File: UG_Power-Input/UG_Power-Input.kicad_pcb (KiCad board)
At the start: 2 copper layers, 109.2 x 68.6 mm, 46 parts, among them J1 12V IN, J2 12V OUT, J3 5V OUT, U1 LM2679

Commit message: PCB rendering added
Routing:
- net GND: vias 120 -> 166
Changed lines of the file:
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@@
     (thickness 1.6002)
     (drawings 66)
-    (tracks 132)
+    (tracks 178)
     (zones 0)
     (modules 46)
@@
     (38 B.Mask user)
     (39 F.Mask user)
+    (41 Cmts.User user)
     (44 Edge.Cuts user)
     (45 Margin user)
-    (46 B.CrtYd user)
-    (47 F.CrtYd user)
+    (46 B.CrtYd user hide)
+    (47 F.CrtYd user hide)
     (49 F.Fab user hide)
   )
@@
     (solder_mask_min_width 0.1)
     (aux_axis_origin 102.87 62.484)
-    (grid_origin 102.87 62.484)
+    (grid_origin 209.042 100.076)
     (visible_elements FFFFFFFF)
     (pcbplotparams
@@
     (tags "mounting hole 3.5mm")
     (attr virtual)
-    (fp_text reference H3 (at 5.334 0) (layer B.SilkS)
-      (effects (font (size 1 1) (thickness 0.15)) (justify mirror))
-    )
-    (fp_text value 3.5mm (at 6.858 0) (layer F.SilkS)
+    (fp_text reference H3 (at 5.334 0.762) (layer B.SilkS)
+      (effects (font (size 1 1) (thickness 0.15)) (justify mirror))
+    )
+    (fp_text value 3.5mm (at 6.858 0.762) (layer F.SilkS)
       (effects (font (size 1 1) (thickness 0.15)))
     )
@@
   (gr_line (start 119.126 94.234) (end 119.126 86.106) (layer B.SilkS) (width 0.3))
   (gr_line (start 111.252 94.234) (end 119.126 94.234) (layer B.SilkS) (width 0.3))
-  (dimension 68.58 (width 0.1524) (layer F.Fab)
-    (gr_text "68.580 mm" (at 218.4908 96.774 270) (layer F.Fab)
+  (dimension 68.58 (width 0.1524) (layer Cmts.User)
+    (gr_text "68.580 mm" (at 218.4908 96.774 -90) (layer Cmts.User)
       (effects (font (size 1.016 1.016) (thickness 0.1524)))
     )
@@
     (arrow2b (pts (xy 217.17 62.484) (xy 217.756421 63.610504)))
   )
-  (dimension 109.22 (width 0.1524) (layer F.Fab)
-    (gr_text "109.220 mm" (at 157.48 56.0832) (layer F.Fab)
+  (dimension 109.22 (width 0.1524) (layer Cmts.User)
+    (gr_text "109.220 mm" (at 157.48 56.0832) (layer Cmts.User)
       (effects (font (size 1.016 1.016) (thickness 0.1524)))
     )
@@
   (via (at 209.042 102.616) (size 0.8) (drill 0.4) (layers Front Back) (net 1))
   (via (at 209.042 100.076) (size 0.8) (drill 0.4) (layers Front Back) (net 1))
-  (via (at 203.962 95.758) (size 0.8) (drill 0.4) (layers Front Back) (net 1))
-  (via (at 203.962 90.678) (size 0.8) (drill 0.4) (layers Front Back) (net 1))
-  (via (at 206.502 98.298) (size 0.8) (drill 0.4) (layers Front Back) (net 1))
-  (via (at 203.962 88.138) (size 0.8) (drill 0.4) (layers Front Back) (net 1))
+  (via (at 203.962 94.996) (size 0.8) (drill 0.4) (layers Front Back) (net 1))
+  (via (at 203.962 89.916) (size 0.8) (drill 0.4) (layers Front Back) (net 1))
+  (via (at 206.502 97.536) (size 0.8) (drill 0.4) (layers Front Back) (net 1))
+  (via (at 203.962 87.376) (size 0.8) (drill 0.4) (layers Front Back) (net 1))
   (via (at 201.422 83.058) (size 0.8) (drill 0.4) (layers Front Back) (net 1))
   (via (at 203.962 80.518) (size 0.8) (drill 0.4) (layers Front Back) (net 1))
   (via (at 206.502 77.978) (size 0.8) (drill 0.4) (layers Front Back) (net 1))
-  (via (at 206.502 72.898) (size 0.8) (drill 0.4) (layers Front Back) (net 1))
+  (via (at 206.502 72.136) (size 0.8) (drill 0.4) (layers Front Back) (net 1))
   (via (at 197.104 67.564) (size 0.8) (drill 0.4) (layers Front Back) (net 1))
   (via (at 199.644 67.564) (size 0.8) (drill 0.4) (layers Front Back) (net 1))
   (via (at 202.184 67.564) (size 0.8) (drill 0.4) (layers Front Back) (net 1))
   (via (at 197.104 65.024) (size 0.8) (drill 0.4) (layers Front Back) (net 1))
+  (via (at 135.128 64.516) (size 0.8) (drill 0.4) (layers Front Back) (net 1))
+  (via (at 132.588 64.516) (size 0.8) (drill 0.4) (layers Front Back) (net 1))
+  (via (at 130.048 64.516) (size 0.8) (drill 0.4) (layers Front Back) (net 1))
+  (via (at 127.508 64.516) (size 0.8) (drill 0.4) (layers Front Back) (net 1))
+  (via (at 124.968 64.516) (size 0.8) (drill 0.4) (layers Front Back) (net 1))
+  (via (at 122.428 64.516) (size 0.8) (drill 0.4) (layers Front Back) (net 1))
+  (via (at 119.888 64.516) (size 0.8) (drill 0.4) (layers Front Back) (net 1))
+  (via (at 117.348 64.516) (size 0.8) (drill 0.4) (layers Front Back) (net 1))
+  (via (at 114.808 64.516) (size 0.8) (drill 0.4) (layers Front Back) (net 1))
+  (via (at 112.268 64.516) (size 0.8) (drill 0.4) (layers Front Back) (net 1))
+  (via (at 112.268 67.056) (size 0.8) (drill 0.4) (layers Front Back) (net 1))
+  (via (at 112.268 69.596) (size 0.8) (drill 0.4) (layers Front Back) (net 1))
+  (via (at 112.268 72.136) (size 0.8) (drill 0.4) (layers Front Back) (net 1))
+  (via (at 109.728 72.136) (size 0.8) (drill 0.4) (layers Front Back) (net 1))
+  (via (at 107.188 72.136) (size 0.8) (drill 0.4) (layers Front Back) (net 1))
+  (via (at 104.648 72.136) (size 0.8) (drill 0.4) (layers Front Back) (net 1))
+  (via (at 104.648 74.676) (size 0.8) (drill 0.4) (layers Front Back) (net 1))
+  (via (at 104.648 77.216) (size 0.8) (drill 0.4) (layers Front Back) (net 1))
+  (via (at 135.128 129.032) (size 0.8) (drill 0.4) (layers Front Back) (net 1))
+  (via (at 132.588 129.032) (size 0.8) (drill 0.4) (layers Front Back) (net 1))
+  (via (at 130.048 129.032) (size 0.8) (drill 0.4) (layers Front Back) (net 1))
+  (via (at 127.508 129.032) (size 0.8) (drill 0.4) (layers Front Back) (net 1))
+  (via (at 124.968 129.032) (size 0.8) (drill 0.4) (layers Front Back) (net 1))
+  (via (at 122.428 129.032) (size 0.8) (drill 0.4) (layers Front Back) (net 1))
+  (via (at 119.888 129.032) (size 0.8) (drill 0.4) (layers Front Back) (net 1))
+  (via (at 117.348 129.032) (size 0.8) (drill 0.4) (layers Front Back) (net 1))
+  (via (at 114.808 129.032) (size 0.8) (drill 0.4) (layers Front Back) (net 1))
+  (via (at 112.268 129.032) (size 0.8) (drill 0.4) (layers Front Back) (net 1))
+  (via (at 112.268 126.492) (size 0.8) (drill 0.4) (layers Front Back) (net 1))
+  (via (at 112.268 123.952) (size 0.8) (drill 0.4) (layers Front Back) (net 1))
+  (via (at 112.268 121.412) (size 0.8) (drill 0.4) (layers Front Back) (net 1))
+  (via (at 109.728 121.412) (size 0.8) (drill 0.4) (layers Front Back) (net 1))
+  (via (at 104.648 121.412) (size 0.8) (drill 0.4) (layers Front Back) (net 1))
+  (via (at 104.648 118.872) (size 0.8) (drill 0.4) (layers Front Back) (net 1))
+  (via (at 104.648 116.332) (size 0.8) (drill 0.4) (layers Front Back) (net 1))
+  (via (at 158.75 129.032) (size 0.8) (drill 0.4) (layers Front Back) (net 1))
+  (via (at 161.29 129.032) (size 0.8) (drill 0.4) (layers Front Back) (net 1))
+  (via (at 163.83 129.032) (size 0.8) (drill 0.4) (layers Front Back) (net 1))
+  (via (at 209.042 97.536) (size 0.8) (drill 0.4) (layers Front Back) (net 1))
+  (via (at 209.042 94.996) (size 0.8) (drill 0.4) (layers Front Back) (net 1))
+  (via (at 209.042 89.916) (size 0.8) (drill 0.4) (layers Front Back) (net 1))
+  (via (at 209.042 87.376) (size 0.8) (drill 0.4) (layers Front Back) (net 1))
+  (via (at 209.042 84.836) (size 0.8) (drill 0.4) (layers Front Back) (net 1))
+  (via (at 209.042 79.756) (size 0.8) (drill 0.4) (layers Front Back) (net 1))
+  (via (at 209.042 77.216) (size 0.8) (drill 0.4) (layers Front Back) (net 1))
+  (via (at 209.042 72.136) (size 0.8) (drill 0.4) (layers Front Back) (net 1))
   (segment (start 193.294 110.744) (end 196.088 110.744) (width 2) (layer Front) (net 3))
   (segment (start 193.294 115.824) (end 196.088 115.824) (width 2) (layer Front) (net 5))
@@
     (polygon
       (pts
-        (xy 122.428 96.52) (xy 103.378 96.52) (xy 103.378 80.772) (xy 122.428 80.772)
+        (xy 122.428 96.52) (xy 102.87 96.52) (xy 102.87 80.772) (xy 122.428 80.772)
       )
     )
@@
     (polygon
       (pts
-        (xy 122.428 112.776) (xy 103.378 112.776) (xy 103.378 97.028) (xy 122.428 97.028)
+        (xy 122.428 112.776) (xy 102.87 112.776) (xy 102.87 97.028) (xy 122.428 97.028)
       )
     )

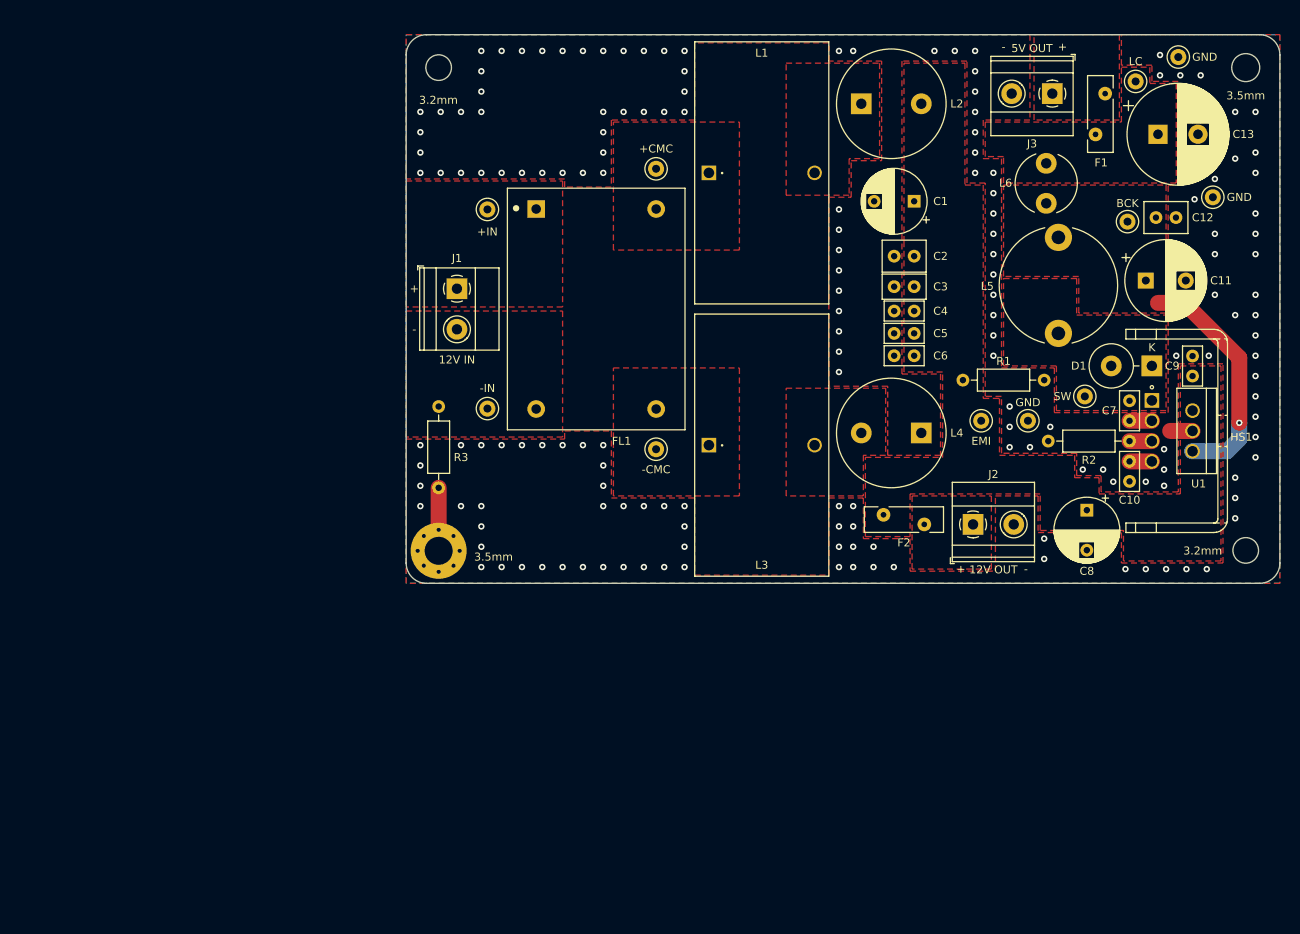
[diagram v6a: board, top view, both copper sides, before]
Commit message: Changes to terminal blocks
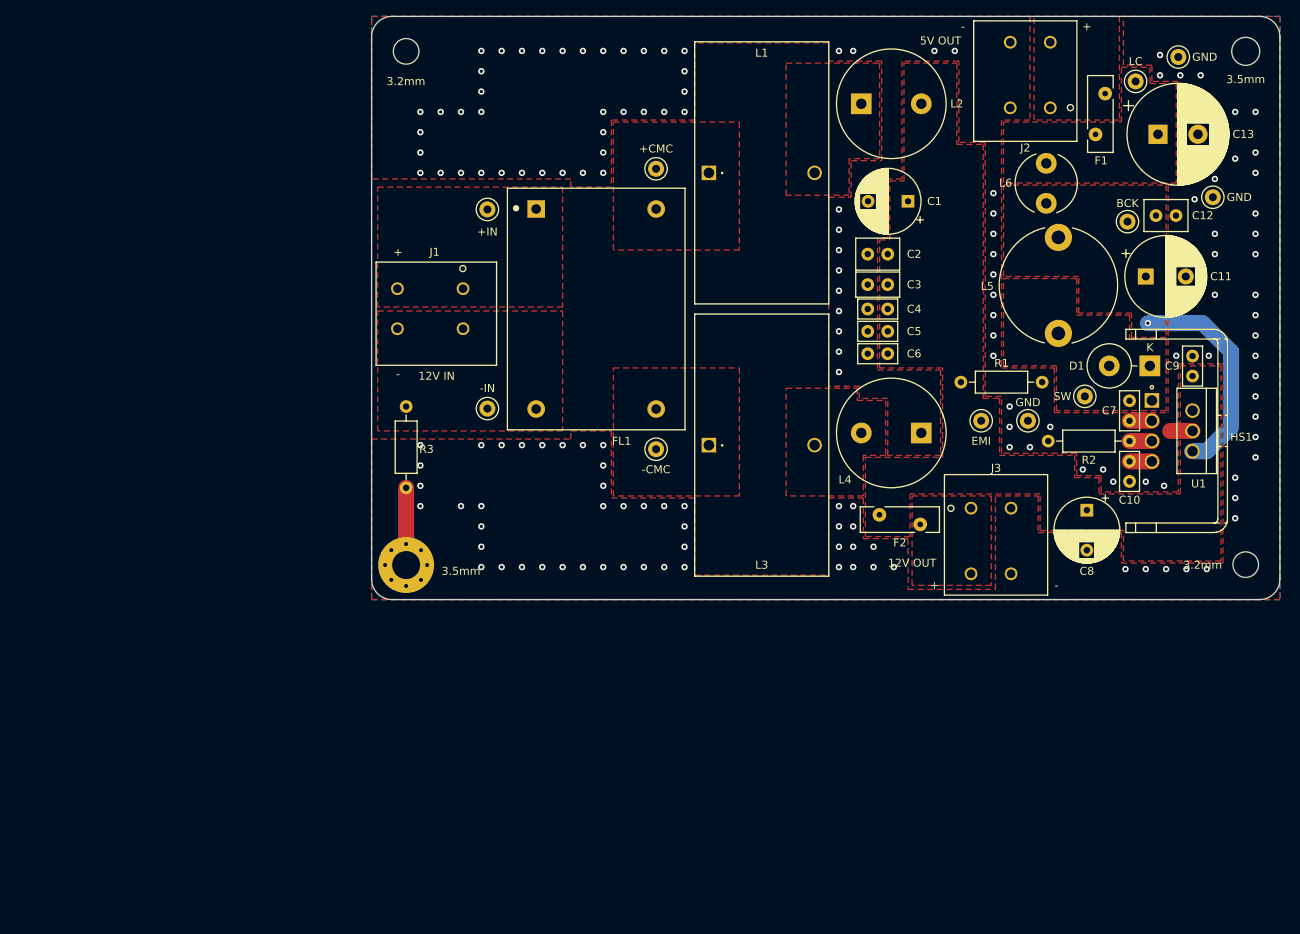
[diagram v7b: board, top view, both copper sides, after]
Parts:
- J1: footprint TerminalBlock_Phoenix:TerminalBlock_Phoenix_MKDS-1,5-2-5.08_1x02_P5.08mm_Horizontal -> TerminalBlock_Weidemueller:TerminalBlock_Weidemueller_LMF-1330180000_1x02_P5.00mm_Vertical
- J2: value 12V OUT -> 5V OUT; footprint TerminalBlock_Phoenix:TerminalBlock_Phoenix_MKDS-1,5-2-5.08_1x02_P5.08mm_Horizontal -> TerminalBlock_Weidemueller:TerminalBlock_Weidemueller_LMF-1330180000_1x02_P5.00mm_Vertical
- J3: value 5V OUT -> 12V OUT; footprint TerminalBlock_Phoenix:TerminalBlock_Phoenix_MKDS-1,5-2-5.08_1x02_P5.08mm_Horizontal -> TerminalBlock_Weidemueller:TerminalBlock_Weidemueller_LMF-1330180000_1x02_P5.00mm_Vertical
- moved J2 53.0 mm to (183.4, 71.6), turned to 180 degrees
- moved J3 52.8 mm to (173.5, 121.7), turned to 0 degrees
- moved H1 4.54 mm to (102.9, 64.6)
- moved H3 4.44 mm to (102.9, 128.8)
- moved R3 4.06 mm to (102.9, 109.0)
- moved C2 3.31 mm to (163.1, 89.9)
- moved C3 3.31 mm to (163.1, 93.7)
- moved C4 3.31 mm to (163.1, 96.8)
- moved C5 3.31 mm to (163.1, 99.6)
- moved C6 3.31 mm to (163.1, 102.4)
- moved H2 2.03 mm to (207.8, 64.6)
- moved H4 1.78 mm to (207.8, 128.7)
- moved C1 0.76 mm to (165.6, 83.3)
- moved J1 0.76 mm to (110.0, 94.2)
- moved C11 0.51 mm to (195.3, 92.7)
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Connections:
- J1 pad 2: -IN -> Net-(FL1-Pad1)
- J2 pad 1: Net-(F2-Pad1) -> Net-(F1-Pad1)
- J2 pad 2: GND -> Net-(F1-Pad1)
- J3 pad 1: Net-(F1-Pad1) -> Net-(F2-Pad1)
- J3 pad 2: GND -> Net-(F2-Pad1)
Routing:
- net BUCK.OUT: track 29.7 -> 27.4 mm
- net Net-(H3-Pad1): track 7.82 -> 9.65 mm
- net GND: vias 166 -> 152
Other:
- board size 109.2 x 68.6 mm -> 113.5 x 72.9 mm

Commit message: Changes to PCB silkscreen
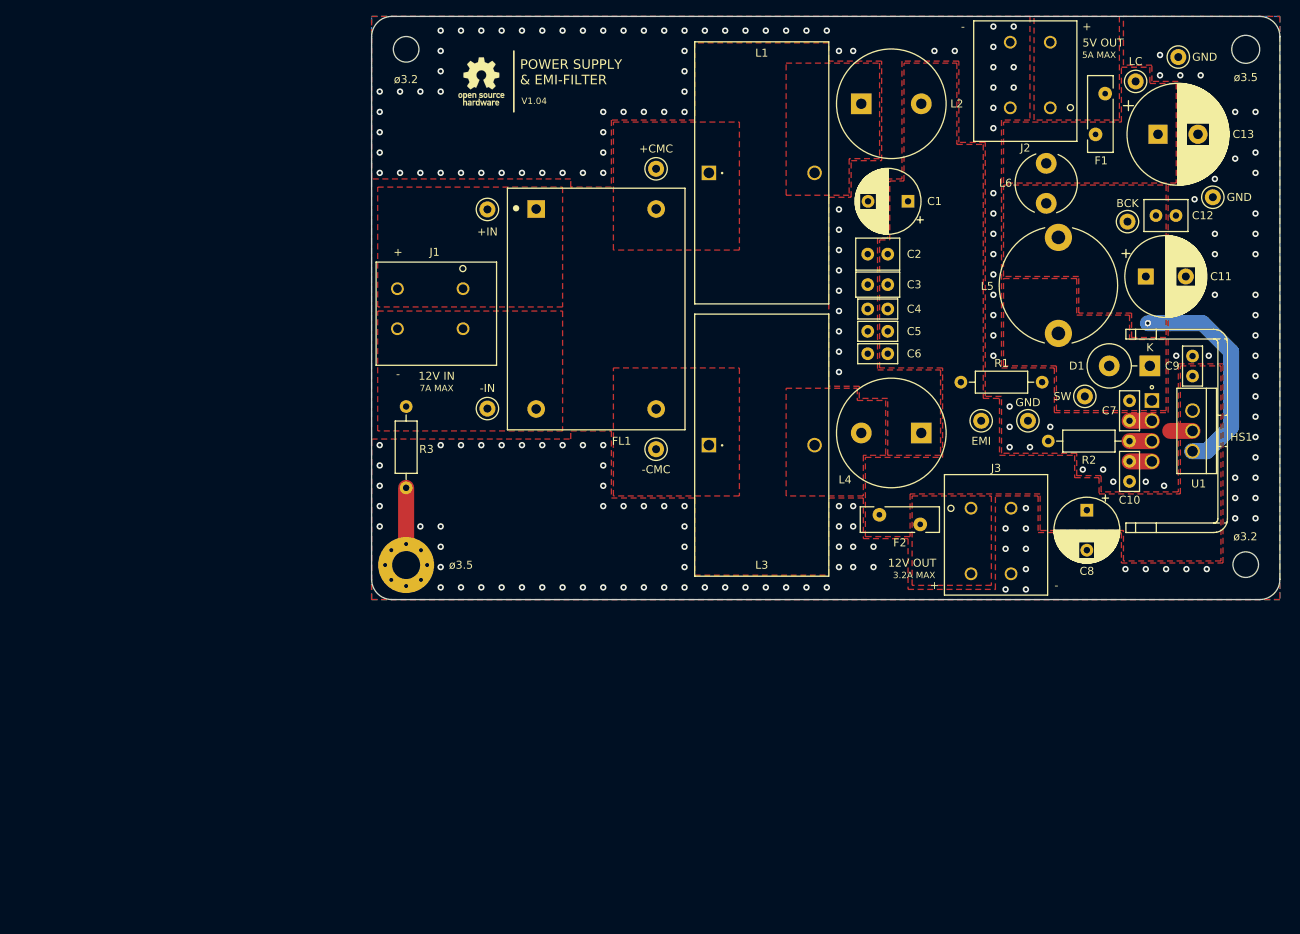
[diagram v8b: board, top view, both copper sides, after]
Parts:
- added REF**: OSHW-Logo_5.7x6mm_SilkScreen, Symbol:OSHW-Logo_5.7x6mm_SilkScreen, F.Cu at (112.3, 68.3)
- H1, H4: value 3.2mm -> ø3.2
- H2, H3: value 3.5mm -> ø3.5
- moved H1 0.25 mm to (102.9, 64.3)
- moved H2 0.25 mm to (207.8, 64.3)
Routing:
- net GND: vias 152 -> 197
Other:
- board text added: "POWER SUPPLY & EMI-FILTER"
- board text added: "V1.04"
